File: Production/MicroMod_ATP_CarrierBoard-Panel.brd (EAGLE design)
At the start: 111.5 x 238.8 mm, 873 parts, among them J19 QWIIC_RIGHT_ANGLE, J2 JTAG, J20 QWIIC_RIGHT_ANGLE, J21 1X04_SMD_STRAIGHT_COMBO, J27 MICROMOD-2222-C, J28 USB_A_SMT_FEMALE, J34 QWIIC_RIGHT_ANGLE, J35 QWIIC_RIGHT_ANGLE, J37 1X04_SMD_STRAIGHT_COMBO, J4 USB_A_SMT_FEMALE, J40 1X04_SMD_STRAIGHT_COMBO, J50 JTAG, J51 MICROMOD-2222-C, J52 USB_A_SMT_FEMALE, J58 QWIIC_RIGHT_ANGLE, J59 QWIIC_RIGHT_ANGLE, J6 MICROMOD-2222-C, J61 1X04_SMD_STRAIGHT_COMBO, J64 1X04_SMD_STRAIGHT_COMBO, J7 JTAG, J74 JTAG, J75 MICROMOD-2222-C, J76 USB_A_SMT_FEMALE, J8 1X04_SMD_STRAIGHT_COMBO, J82 QWIIC_RIGHT_ANGLE, J83 QWIIC_RIGHT_ANGLE, J85 1X04_SMD_STRAIGHT_COMBO, J88 1X04_SMD_STRAIGHT_COMBO, U1 AP7361C-33, U2 AP7361C-33, U3 AP7361C-33, U5 AP7361C-33

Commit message: Update panel
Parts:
- added D21: 3.3V, SparkFun-DiscreteSemi:SOD-323
- added D22, D23: RED, SparkFun-LED:LED-0603
- added D24: 1A/15V/220mV, SparkFun-DiscreteSemi:DO-214BA
- D11, D16: value 3A/10V/280mV -> RED; device SparkFun-DiscreteSemi:SOD-323 -> SparkFun-LED:LED-0603
- D12: value 1A/23V/620mV -> 1A/15V/220mV; device SparkFun-DiscreteSemi:SOD-323 -> SparkFun-DiscreteSemi:DO-214BA
- D13: value 3.3V -> 3A/10V/280mV
- D14, D20: value RED -> 1A/23V/620mV; device SparkFun-LED:LED-0603 -> SparkFun-DiscreteSemi:SOD-323
- D15, D9: value RED -> 3.3V; device SparkFun-LED:LED-0603 -> SparkFun-DiscreteSemi:SOD-323
- D17: value 1A/23V/620mV -> RED; device SparkFun-DiscreteSemi:SOD-323 -> SparkFun-LED:LED-0603
- D18: value 3.3V -> 1A/15V/220mV; device SparkFun-DiscreteSemi:SOD-323 -> SparkFun-DiscreteSemi:DO-214BA
- D19: value RED -> 3A/10V/280mV; device SparkFun-LED:LED-0603 -> SparkFun-DiscreteSemi:SOD-323
- D4: value 3A/10V/280mV -> 1A/15V/220mV; device SparkFun-DiscreteSemi:SOD-323 -> SparkFun-DiscreteSemi:DO-214BA
- D5: value 1A/23V/620mV -> 3A/10V/280mV
- D8: value 3.3V -> 1A/23V/620mV
- U$130: device fl3:#VUSB#10 -> buzzard_labels (9):22229
- U$146: device buzzard_labels (9):22229 -> output:#VHOST#0
- U$186, U$331, U$476: device power:#VUSB#10 -> power:#MEAS#10
- U$187, U$332, U$477: device power:#MEAS#10 -> power:#SDA#4
- U$188, U$333, U$478: device power:#SDA#4 -> power:#SWD#10
- U$189, U$334, U$479: device power:#SWD#10 -> headtop:#I2S_CLK#5
- U$190, U$335, U$480: device headtop:#I2S_CLK#5 -> headtop:#DAT1#4
- U$191, U$336, U$481: device headtop:#DAT1#4 -> headtop:#DAT0#4
- U$192, U$337, U$482: device headtop:#DAT0#4 -> headers_dup:#RX2#3
- U$193, U$338, U$483: device headers_dup:#RX2#3 -> headers_dup:#TX2#2
- U$194, U$339, U$484: device headers_dup:#TX2#2 -> headers_dup:#SCL1#3
- U$195, U$340, U$485: device headers_dup:#SCL1#3 -> headers_dup:#SDA1#3
- U$196, U$341, U$486: device headers_dup:#SDA1#3 -> headers_dup:#SCK1#2
- U$197, U$342, U$487: device headers_dup:#SCK1#2 -> headers_dup:VIN3
- U$198, U$343, U$488: device headers_dup:VIN3 -> headers_dup:3V34
- U$199, U$344, U$489: device headers_dup:3V34 -> power:#3V3#1
- U$203, U$348, U$493: device power:#3V3#1 -> headers_dup:ATP0
- U$204, U$349, U$494: device headers_dup:ATP0 -> headers_dup:I2C4
- U$205, U$350, U$495: device headers_dup:I2C4 -> headers_dup:I2C14
- U$206, U$351, U$496: device headers_dup:I2C14 -> headers_dup:ATP_CARRIER_BOARD1
- U$207, U$352, U$497: device headers_dup:ATP_CARRIER_BOARD1 -> fl1:##CS1##0
- U$208, U$353, U$498: device fl1:##CS1##0 -> headers_dup:#CIPO1#2
- U$209, U$354, U$499: device headers_dup:#CIPO1#2 -> headers_dup:#COPI1#2
- U$210, U$355, U$500: device headers_dup:#COPI1#2 -> headers_dup:##CS1##2
- U$211, U$356, U$501: device headers_dup:##CS1##2 -> power:##RESET##7
- U$212, U$357, U$502: device power:##RESET##7 -> headtop:##CS##0
- U$213, U$358, U$503: device headtop:##CS##0 -> fl1:#CIPO1#2
- U$214, U$359, U$504: device fl1:#CIPO1#2 -> fl1:#COPI1#2
- U$215, U$360, U$505: device fl1:#COPI1#2 -> fl1:#RX2#3
- U$216, U$361, U$506: device fl1:#RX2#3 -> fl1:#SCK1#2
- U$217, U$362, U$507: device fl1:#SCK1#2 -> fl1:#SCL1#3
- U$218, U$363, U$508: device fl1:#SCL1#3 -> fl1:#SDA1#3
- U$219, U$364, U$509: device fl1:#SDA1#3 -> fl1:#TX2#2
- U$220, U$365, U$510: device fl1:#TX2#2 -> fl2:##CS##DAT3#0
- U$221, U$366, U$511: device fl2:##CS##DAT3#0 -> fl2:#DAT2#5
- U$222, U$367, U$512: device fl2:#DAT2#5 -> fl2:#DAT1#5
- U$223, U$368, U$513: device fl2:#DAT1#5 -> fl2:#COPI#4
- U$224, U$369, U$514: device fl2:#COPI#4 -> fl2:#SCK#4
- U$225, U$370, U$515: device fl2:#SCK#4 -> fl2:#MCLK#6
- U$226, U$371, U$516: device fl2:#MCLK#6 -> fl2:#I2S_FS#7
- U$227, U$372, U$517: device fl2:#I2S_FS#7 -> fl2:#I2S_CLK#7
- U$228, U$373, U$518: device fl2:#I2S_CLK#7 -> fl2:#RTS#7
- U$229, U$374, U$519: device fl2:#RTS#7 -> fl2:#CTS#8
- U$230, U$375, U$520: device fl2:#CTS#8 -> fl2:#TX#9
- U$231, U$376, U$521: device fl2:#TX#9 -> fl2:#RX#10
- U$232, U$377, U$522: device fl2:#RX#10 -> fl2:#CAN_RX#10
- U$233, U$378, U$523: device fl2:#CAN_RX#10 -> fl2:#CAN_TX#10
- U$234, U$379, U$524: device fl2:#CAN_TX#10 -> fl4:#D0#0
- U$235, U$380, U$525: device fl4:#D0#0 -> fl3:#GND#0
- U$241, U$386, U$531: device fl3:#GND#0 -> fl3:#3V3#1
- U$243, U$388, U$533: device fl3:#3V3#1 -> fl3:#SDA#4
- U$244, U$389, U$534: device fl3:#SDA#4 -> fl3:#SCL#5
- U$245, U$390, U$535: device fl3:#SCL#5 -> fl2:##I2C_INT##10
- U$246, U$391, U$536: device fl2:##I2C_INT##10 -> fl4:#G11#10
- U$247, U$392, U$537: device fl4:#G11#10 -> fl4:#G8#8
- U$248, U$393, U$538: device fl4:#G8#8 -> fl4:#G7#7
- U$249, U$394, U$539: device fl4:#G7#7 -> fl4:#G6#6
- U$250, U$395, U$540: device fl4:#G6#6 -> fl4:#G5#5
- U$251, U$396, U$541: device fl4:#G5#5 -> fl4:#G4#4
- U$252, U$397, U$542: device fl4:#G4#4 -> fl4:#G3#3
- U$253, U$398, U$543: device fl4:#G3#3 -> fl4:#G2#2
- U$254, U$399, U$544: device fl4:#G2#2 -> fl4:#G1#2
- U$255, U$400, U$545: device fl4:#G1#2 -> fl4:#G0#2
- U$256, U$401, U$546: device fl4:#G0#2 -> fl4:#PWM0#10
- U$257, U$402, U$547: device fl4:#PWM0#10 -> fl4:#PWM1#10
- U$258, U$403, U$548: device fl4:#PWM1#10 -> fl4:#A0#10
- U$259, U$404, U$549: device fl4:#A0#10 -> fl4:#A1#10
- U$260, U$405, U$550: device fl4:#A1#10 -> fl3:##RESET##7
- U$261, U$406, U$551: device fl3:##RESET##7 -> fl3:#3V3#1
- U$262, U$407, U$552: device fl3:#3V3#1 -> fl3:#VIN#6
- U$263, U$408, U$553: device fl3:#VIN#6 -> fl3:#HOST_D##9
- U$264, U$409, U$554: device fl3:#HOST_D##9 -> fl3:#HOST_D##10
- U$265, U$410, U$555: device fl3:#HOST_D##10 -> fl3:#SWD#10
- U$266, U$411, U$556: device fl3:#VUSB#10 -> fl3:#MEAS#10
- U$267, U$412, U$557: device fl3:#SWD#10 -> fl3:#VIN_LED#10
- U$268, U$413, U$558: device fl3:#MEAS#10 -> fl3:#3V3_LED#10
- U$269, U$414, U$559: device fl3:#VIN_LED#10 -> fl4:#G9#ADC##CAM_HSYNC#9
- U$270, U$415, U$560: device fl3:#3V3_LED#10 -> fl4:#G10#ADC##CAM_VSYNC#10
- U$271, U$416, U$561: device fl4:#G9#ADC##CAM_HSYNC#9 -> fl2:#I2S_SDI#CAM_PCLK#7
- U$272, U$417, U$562: device fl4:#G10#ADC##CAM_VSYNC#10 -> fl2:#I2S_SDO#CAM_MCLK#7
- U$273, U$418, U$563: device fl2:#I2S_SDI#CAM_PCLK#7 -> fl3:#3V3#1
- U$274, U$419, U$564: device fl2:#I2S_SDO#CAM_MCLK#7 -> headtop:#SCK#2
- U$275, U$420, U$565: device fl3:#3V3#1 -> power:#GND#0
- U$276, U$421, U$566: device headtop:#SCK#2 -> power:#GND#0
- U$278, U$423, U$568: device power:#GND#0 -> headtop:##I2C_INT##10
- U$279, U$424, U$569: device power:#GND#0 -> D1:D10
- U$280, U$425, U$570: device headtop:##I2C_INT##10 -> SparkFun-MicroMod:MICROMOD_MI_LOGO_1
- U$281, U$426, U$571: device D1:D10 -> headtop:MOUNT10
- U$282, U$427, U$572: device SparkFun-MicroMod:MICROMOD_MI_LOGO_1 -> headtop:MOUNT10
- U$285, U$430, U$575: device headtop:MOUNT10 -> SparkFun-MicroMod:MICROMOD_LOGO_1
- U$286, U$431, U$576: device headtop:MOUNT10 -> fl2:#CIPO#DAT0#6
- U$287, U$432, U$577: device SparkFun-MicroMod:MICROMOD_LOGO_1 -> D1_again:D10
- U$288, U$433, U$578: device fl2:#CIPO#DAT0#6 -> output:#EN#0
- U$289, U$434, U$579: device D1_again:D10 -> output:#VHOST#0
- U$290, U$435, U$580: device output:#EN#0 -> output:#VHOST#0
- U$50: device power:#VUSB#10 -> output:#VHOST#0
- moved D11 105.7 mm to (6.60, 63.2)
- moved D17 104.3 mm to (6.60, 119.6)
- moved D16 104.0 mm to (6.60, 121.7)
- moved D4 92.8 mm to (2.72, 26.0), turned to 90 degrees
- moved D12 91.6 mm to (2.72, 82.4), turned to 90 degrees
- moved U$275 78.3 mm to (76.8, 71.6), flipped to the top, turned to 0 degrees
- moved U$420 78.3 mm to (76.8, 128.0), flipped to the top, turned to 0 degrees
- moved U$565 78.3 mm to (76.8, 184.4), flipped to the top, turned to 0 degrees
- moved U$277 72.9 mm to (10.9, 102.7), turned to 90 degrees
- moved U$422 72.9 mm to (10.9, 159.1), turned to 90 degrees
- moved U$567 72.9 mm to (10.9, 215.5), turned to 90 degrees
- moved U$202 70.5 mm to (7.62, 102.9), turned to 90 degrees
- moved U$347 70.5 mm to (7.62, 159.3), turned to 90 degrees
- moved U$492 70.5 mm to (7.62, 215.6), turned to 90 degrees
- moved U$203 68.7 mm to (69.1, 72.1), turned to 0 degrees
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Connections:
- removed net N$19 (its old number): BT3.+, D11.A, R19.1
- removed net N$20 (its old number): D14.A, R23.1
- removed net N$28 (its old number): D19.A, R31.1
- removed net N$29 (its old number): D20.A, R32.1
- removed net N$8 (its old number): BT2.+, D4.A, R11.1
- new net N$16: D11.C, VIN_LED1.1
- new net N$18: D12.C, J28.VBUS, J42.1
- new net N$24: 3V3_LED2.1, D16.C
- new net N$25: D17.C, VIN_LED2.1
- new net N$32: D23.A, R32.1
- new net N$33: 3V3_LED3.1, D22.C
- new net N$34: D23.C, VIN_LED3.1
- new net N$36: D24.C, J76.VBUS, J90.1
- new net N$7: D4.C, J11.1, J4.VBUS
- net 3.3V1: now also D8.A; no longer D5.A
- net 3.3V2: now also D14.A; no longer D12.A
- net 3.3V3: now also D20.A; no longer D17.A
- net 3.3V_EN1: now also D9.C; no longer D8.C
- net 3.3V_EN2: now also D15.C; no longer D13.C
- net 3.3V_EN3: now also D21.C; no longer D18.C
- net GND1: now also D9.A; no longer D8.A
- net GND2: now also D15.A; no longer D13.A
- net GND3: now also D21.A; no longer D18.A
- net N$12: now also R15.1; no longer R16.1
- net N$13: now also D11.A, R16.1; no longer 3V3_LED1.1, D9.C
- net N$15: now also 3V3_LED1.1; no longer VIN_LED1.1
- net N$21: now also BT3.+, D13.A, R19.1; no longer D15.A, R24.1
- net N$22: now also D16.A, R23.1; no longer 3V3_LED2.1, D14.C
- net N$23: now also D17.A, R24.1; no longer D15.C, VIN_LED2.1
- net N$27: now also D18.C, J52.VBUS, J66.1; no longer BT4.+, D16.A, R27.1
- net N$30: now also BT4.+, D19.A, R27.1; no longer 3V3_LED3.1, D19.C
- net N$31: now also D22.A, R31.1; no longer D20.C, VIN_LED3.1
- net N$9: now also BT2.+, D5.A, R11.1; no longer D9.A, R15.1
- net RTC_3V1: now also D8.C; no longer D4.C
- net RTC_3V2: now also D13.C, D14.C; no longer D11.C, D12.C
- net RTC_3V3: now also D19.C, D20.C; no longer D16.C, D17.C
- net V_USB: now also D4.A; no longer J11.1, J4.VBUS
- net V_USB1: now also D12.A; no longer J28.VBUS, J42.1
- net V_USB2: now also D18.A; no longer J52.VBUS, J66.1
- net V_USB3: now also D24.A; no longer J76.VBUS, J90.1
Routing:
- net N$36: track 0.00 -> 25.8 mm
- net N$18: track 0.00 -> 25.8 mm
- net N$7: track 0.00 -> 25.8 mm
- net N$27: track 4.10 -> 25.8 mm
- net V_USB1: track 45.7 -> 25.5 mm
- net V_USB: track 45.7 -> 25.5 mm
- net V_USB2: track 45.7 -> 25.5 mm
- net V_USB3: track 45.7 -> 25.5 mm
- net N$19 (its old number): track 4.10 -> 0.00 mm
- net N$8 (its old number): track 4.10 -> 0.00 mm
- net N$34: track 0.00 -> 2.67 mm, vias 0 -> 1
- net N$33: track 0.00 -> 2.67 mm, vias 0 -> 1
- net N$25: track 0.00 -> 2.67 mm, vias 0 -> 1
- net N$24: track 0.00 -> 2.67 mm, vias 0 -> 1
- net N$16: track 0.00 -> 2.67 mm, vias 0 -> 1
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
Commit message: Changes production board size to 2x2 instead of 1x4
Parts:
- moved BYP3 143.9 mm to (100.8, 84.0)
- moved C22 143.9 mm to (104.1, 69.6)
- moved C23 143.9 mm to (105.7, 69.6)
- moved C24 143.9 mm to (107.2, 69.6)
- moved D19 143.9 mm to (153.9, 95.2)
- moved D24 143.9 mm to (92.1, 82.4)
- moved FD14 143.9 mm to (171.1, 107.7)
- moved FD16 143.9 mm to (171.1, 107.7)
- moved H24 143.9 mm to (173.2, 58.9)
- moved J75 143.9 mm to (125.0, 84.3)
- moved LOGO24 143.9 mm to (153.2, 83.2)
- moved LOGO28 143.9 mm to (157.7, 79.8)
- moved R25 143.9 mm to (97.0, 76.7)
- moved R27 143.9 mm to (153.9, 96.9)
- moved R28 143.9 mm to (105.2, 78.2)
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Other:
- board size 111.5 x 238.8 mm -> 200.9 x 126 mm

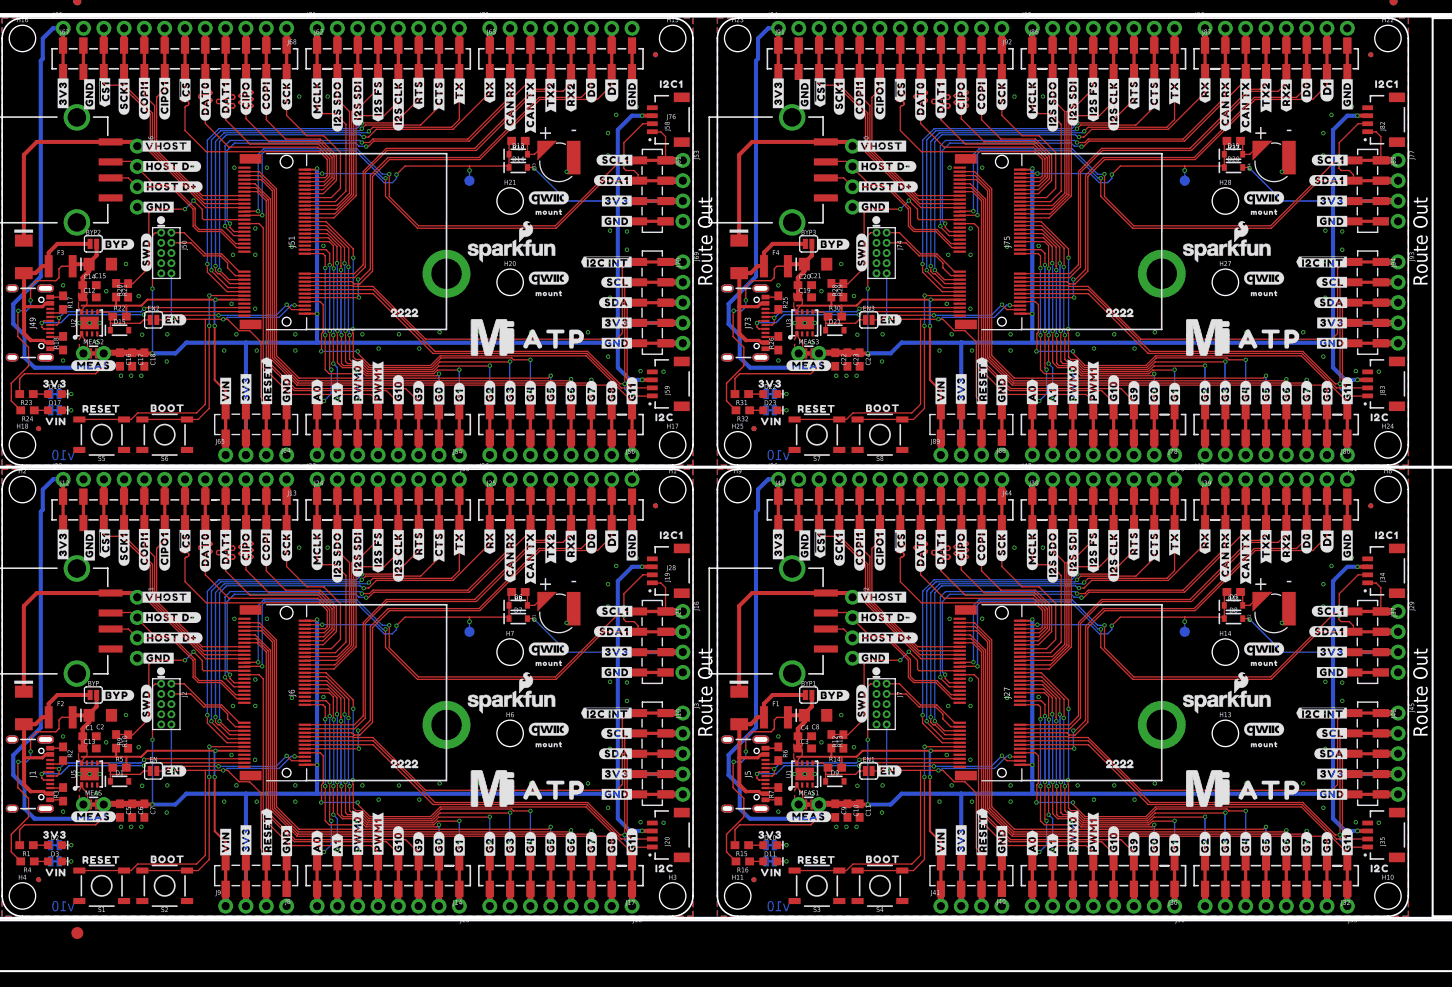
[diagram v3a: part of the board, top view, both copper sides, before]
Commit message: Updates production files with new silk and qwiic connector fixes
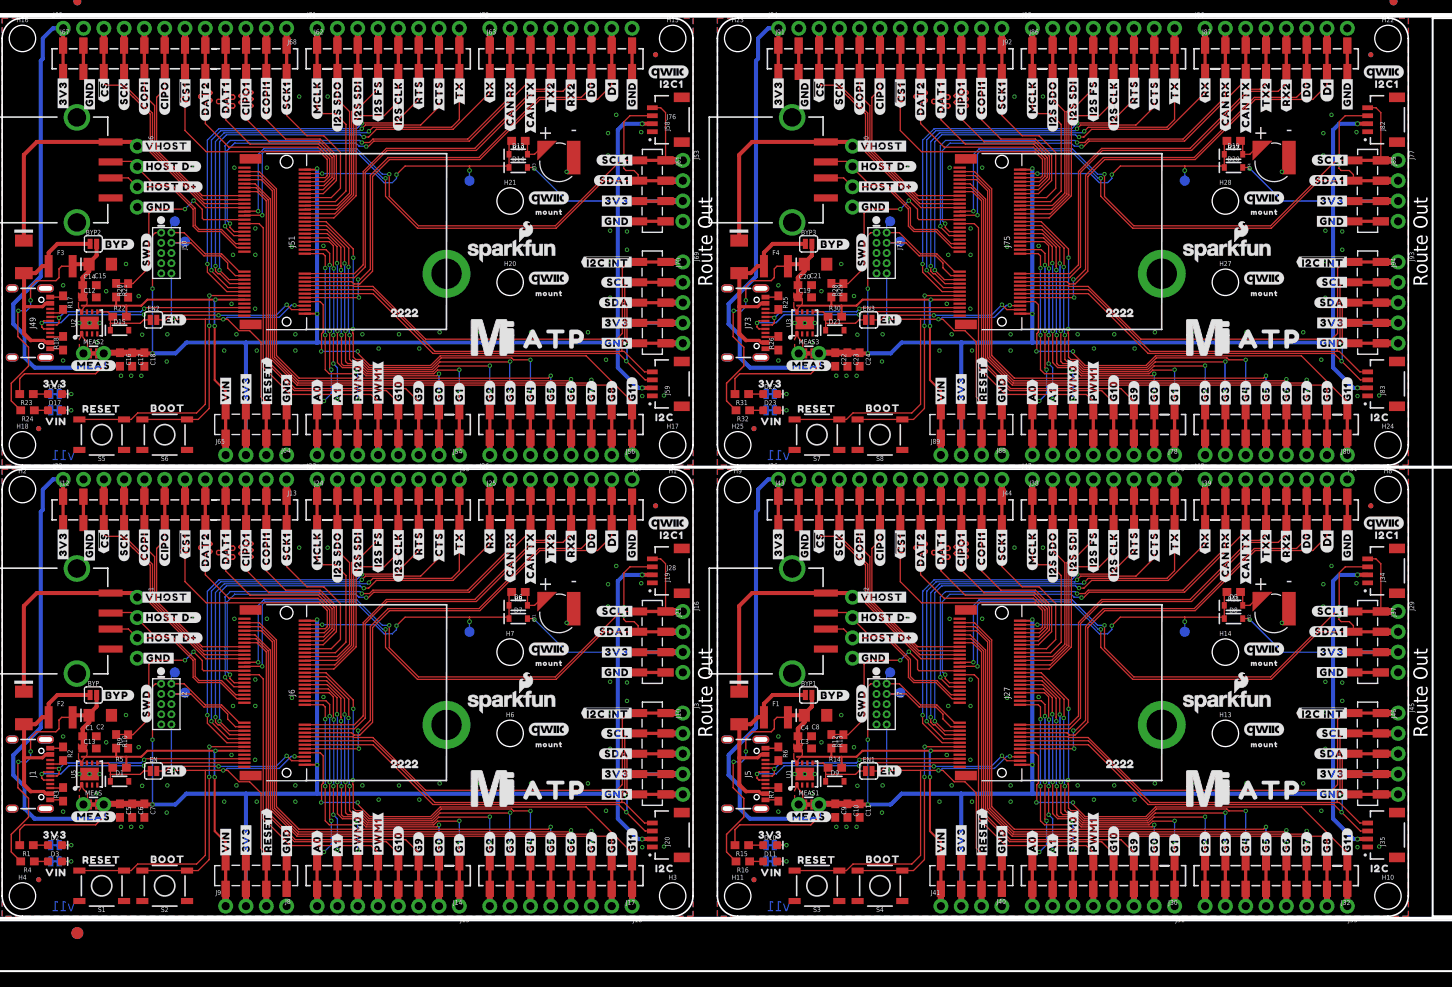
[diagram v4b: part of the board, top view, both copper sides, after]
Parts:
- added E$6: (no value), SparkFun-Retired:FIDUCIAL-1.5X3
- added LOGO29, LOGO30, LOGO32: QWIIC_LOGO_3MM, SparkFun-Aesthetics:QWIIC_5MM
- added LOGO31: QWIIC_LOGO_5MM, SparkFun-Aesthetics:QWIIC_5MM
- added TP10, TP11, TP12, TP5, TP6, TP7, TP8, TP9: TEST-POINT3X5, SparkFun-Connectors:PAD.03X.05
- LOGO10: value SFE_LOGO_NAME_FLAME.1_INCH -> SFE_LOGO_NAME_FLAME.2_INCH; device SparkFun-Aesthetics:SFE_LOGO_NAME_FLAME_.1 -> SparkFun-Aesthetics:SFE_LOGO_NAME_FLAME_.2
- LOGO11, LOGO19, LOGO27: value QWIIC_LOGO_3MM -> SFE_LOGO_NAME_FLAME.1_INCH; device SparkFun-Aesthetics:QWIIC_5MM -> SparkFun-Aesthetics:SFE_LOGO_NAME_FLAME_.1
- LOGO14, LOGO21, LOGO28: value QWIIC_LOGO_5MM -> QWIIC_LOGO_3MM
- LOGO15: value OSHW-LOGOMINI -> QWIIC_LOGO_5MM; device SparkFun-Aesthetics:OSHW-LOGO-MINI -> SparkFun-Aesthetics:QWIIC_5MM
- LOGO16: value SFE_LOGO_NAME_FLAME.2_INCH -> QWIIC_LOGO_3MM; device SparkFun-Aesthetics:SFE_LOGO_NAME_FLAME_.2 -> SparkFun-Aesthetics:QWIIC_5MM
- LOGO17: value SFE_LOGO_NAME_FLAME.1_INCH -> OSHW-LOGOMINI; device SparkFun-Aesthetics:SFE_LOGO_NAME_FLAME_.1 -> SparkFun-Aesthetics:OSHW-LOGO-MINI
- LOGO18, LOGO26: value QWIIC_LOGO_3MM -> SFE_LOGO_NAME_FLAME.2_INCH; device SparkFun-Aesthetics:QWIIC_5MM -> SparkFun-Aesthetics:SFE_LOGO_NAME_FLAME_.2
- LOGO22, LOGO7: value OSHW-LOGOMINI -> QWIIC_LOGO_3MM; device SparkFun-Aesthetics:OSHW-LOGO-MINI -> SparkFun-Aesthetics:QWIIC_5MM
- LOGO23: value SFE_LOGO_NAME_FLAME.2_INCH -> QWIIC_LOGO_5MM; device SparkFun-Aesthetics:SFE_LOGO_NAME_FLAME_.2 -> SparkFun-Aesthetics:QWIIC_5MM
- LOGO24: value SFE_LOGO_NAME_FLAME.1_INCH -> QWIIC_LOGO_3MM; device SparkFun-Aesthetics:SFE_LOGO_NAME_FLAME_.1 -> SparkFun-Aesthetics:QWIIC_5MM
- LOGO25: value QWIIC_LOGO_3MM -> OSHW-LOGOMINI; device SparkFun-Aesthetics:QWIIC_5MM -> SparkFun-Aesthetics:OSHW-LOGO-MINI
- LOGO9: value SFE_LOGO_NAME_FLAME.2_INCH -> OSHW-LOGOMINI; device SparkFun-Aesthetics:SFE_LOGO_NAME_FLAME_.2 -> SparkFun-Aesthetics:OSHW-LOGO-MINI
- U$130: device buzzard_labels (9):22229 -> headtop:#CAN_RX#9
- U$147: device headtop:#CAN_RX#9 -> alc:#CIPO#5178038
- U$190, U$335, U$480: device headtop:#DAT1#4 -> headers_dup:#RX2#3
- U$191, U$336, U$481: device headtop:#DAT0#4 -> headers_dup:#TX2#2
- U$192, U$337, U$482: device headers_dup:#RX2#3 -> headers_dup:#SCL1#3
- U$193, U$338, U$483: device headers_dup:#TX2#2 -> headers_dup:#SDA1#3
- U$194, U$339, U$484: device headers_dup:#SCL1#3 -> headers_dup:#SCK1#2
- U$195, U$340, U$485: device headers_dup:#SDA1#3 -> headers_dup:VIN3
- U$196, U$341, U$486: device headers_dup:#SCK1#2 -> headers_dup:3V34
- U$197, U$342, U$487: device headers_dup:VIN3 -> power:#3V3#1
- U$198, U$343, U$488: device headers_dup:3V34 -> power:#3V3#1
- U$20: device headers_dup:##CS1##2 -> alc:##CS1##5178039
- U$201, U$346, U$491: device power:#3V3#1 -> headers_dup:ATP0
- U$202, U$347, U$492: device power:#3V3#1 -> headers_dup:I2C4
- U$203, U$348, U$493: device headers_dup:ATP0 -> headers_dup:I2C14
- U$204, U$349, U$494: device headers_dup:I2C4 -> headers_dup:ATP_CARRIER_BOARD1
- U$205, U$350, U$495: device headers_dup:I2C14 -> headers_dup:#COPI1#2
- U$206, U$351, U$496: device headers_dup:ATP_CARRIER_BOARD1 -> power:##RESET##7
- U$207, U$352, U$497: device fl1:##CS1##0 -> headtop:##CS##0
- U$208, U$353, U$498: device headers_dup:#CIPO1#2 -> fl1:#COPI1#2
- U$209, U$354, U$499: device headers_dup:#COPI1#2 -> fl1:#RX2#3
- U$210, U$355, U$500: device headers_dup:##CS1##2 -> fl1:#SCK1#2
- U$211, U$356, U$501: device power:##RESET##7 -> fl1:#SCL1#3
- U$212, U$357, U$502: device headtop:##CS##0 -> fl1:#SDA1#3
- U$213, U$358, U$503: device fl1:#CIPO1#2 -> fl1:#TX2#2
- U$214, U$359, U$504: device fl1:#COPI1#2 -> fl2:#DAT2#5
- U$215, U$360, U$505: device fl1:#RX2#3 -> fl2:#DAT1#5
- U$216, U$361, U$506: device fl1:#SCK1#2 -> fl2:#COPI#4
- U$217, U$362, U$507: device fl1:#SCL1#3 -> fl2:#SCK#4
- U$218, U$363, U$508: device fl1:#SDA1#3 -> fl2:#MCLK#6
- U$219, U$364, U$509: device fl1:#TX2#2 -> fl2:#I2S_FS#7
- U$220, U$365, U$510: device fl2:##CS##DAT3#0 -> fl2:#I2S_CLK#7
- U$221, U$366, U$511: device fl2:#DAT2#5 -> fl2:#RTS#7
- U$222, U$367, U$512: device fl2:#DAT1#5 -> fl2:#CTS#8
- U$223, U$368, U$513: device fl2:#COPI#4 -> fl2:#TX#9
- U$224, U$369, U$514: device fl2:#SCK#4 -> fl2:#RX#10
- U$225, U$370, U$515: device fl2:#MCLK#6 -> fl2:#CAN_RX#10
- U$226, U$371, U$516: device fl2:#I2S_FS#7 -> fl2:#CAN_TX#10
- U$227, U$372, U$517: device fl2:#I2S_CLK#7 -> fl4:#D0#0
- U$228, U$373, U$518: device fl2:#RTS#7 -> fl3:#GND#0
- U$229, U$374, U$519: device fl2:#CTS#8 -> fl3:#GND#0
- U$230, U$375, U$520: device fl2:#TX#9 -> fl3:#GND#0
- U$231, U$376, U$521: device fl2:#RX#10 -> fl3:#GND#0
- U$232, U$377, U$522: device fl2:#CAN_RX#10 -> fl3:#GND#0
- U$233, U$378, U$523: device fl2:#CAN_TX#10 -> fl3:#GND#0
- U$234, U$379, U$524: device fl4:#D0#0 -> fl3:#3V3#1
- U$235, U$380, U$525: device fl3:#GND#0 -> fl3:#3V3#1
- U$236, U$381, U$526: device fl3:#GND#0 -> fl3:#SDA#4
- U$237, U$382, U$527: device fl3:#GND#0 -> fl3:#SCL#5
- U$238, U$383, U$528: device fl3:#GND#0 -> fl2:##I2C_INT##10
- U$239, U$384, U$529: device fl3:#GND#0 -> fl4:#G11#10
- U$240, U$385, U$530: device fl3:#GND#0 -> fl4:#G8#8
- U$241, U$386, U$531: device fl3:#3V3#1 -> fl4:#G7#7
- U$242, U$387, U$532: device fl3:#3V3#1 -> fl4:#G6#6
- U$243, U$388, U$533: device fl3:#SDA#4 -> fl4:#G5#5
- U$244, U$389, U$534: device fl3:#SCL#5 -> fl4:#G4#4
- U$245, U$390, U$535: device fl2:##I2C_INT##10 -> fl4:#G3#3
- U$246, U$391, U$536: device fl4:#G11#10 -> fl4:#G2#2
- U$247, U$392, U$537: device fl4:#G8#8 -> fl4:#G1#2
- U$248, U$393, U$538: device fl4:#G7#7 -> fl4:#G0#2
- U$249, U$394, U$539: device fl4:#G6#6 -> fl4:#PWM0#10
- U$250, U$395, U$540: device fl4:#G5#5 -> fl4:#PWM1#10
- U$251, U$396, U$541: device fl4:#G4#4 -> fl4:#A0#10
- U$252, U$397, U$542: device fl4:#G3#3 -> fl4:#A1#10
- U$253, U$398, U$543: device fl4:#G2#2 -> fl3:##RESET##7
- U$254, U$399, U$544: device fl4:#G1#2 -> fl3:#3V3#1
- U$255, U$400, U$545: device fl4:#G0#2 -> fl3:#VIN#6
- U$256, U$401, U$546: device fl4:#PWM0#10 -> fl3:#HOST_D##9
- U$257, U$402, U$547: device fl4:#PWM1#10 -> fl3:#HOST_D##10
- U$258, U$403, U$548: device fl4:#A0#10 -> fl3:#SWD#10
- U$259, U$404, U$549: device fl4:#A1#10 -> fl3:#MEAS#10
- U$260, U$405, U$550: device fl3:##RESET##7 -> fl3:#VIN_LED#10
- U$261, U$406, U$551: device fl3:#3V3#1 -> fl3:#3V3_LED#10
- U$262, U$407, U$552: device fl3:#VIN#6 -> fl4:#G9#ADC##CAM_HSYNC#9
- U$263, U$408, U$553: device fl3:#HOST_D##9 -> fl4:#G10#ADC##CAM_VSYNC#10
- U$264, U$409, U$554: device fl3:#HOST_D##10 -> fl2:#I2S_SDI#CAM_PCLK#7
- U$265, U$410, U$555: device fl3:#SWD#10 -> fl2:#I2S_SDO#CAM_MCLK#7
- U$266, U$411, U$556: device fl3:#MEAS#10 -> fl3:#3V3#1
- U$267, U$412, U$557: device fl3:#VIN_LED#10 -> headtop:#SCK#2
- U$268, U$413, U$558: device fl3:#3V3_LED#10 -> power:#GND#0
- U$269, U$414, U$559: device fl4:#G9#ADC##CAM_HSYNC#9 -> power:#GND#0
- U$270, U$415, U$560: device fl4:#G10#ADC##CAM_VSYNC#10 -> power:#GND#0
- U$271, U$416, U$561: device fl2:#I2S_SDI#CAM_PCLK#7 -> headtop:##I2C_INT##10
- U$272, U$417, U$562: device fl2:#I2S_SDO#CAM_MCLK#7 -> D1:D10
- U$273, U$418, U$563: device fl3:#3V3#1 -> SparkFun-MicroMod:MICROMOD_MI_LOGO_1
- U$274, U$419, U$564: device headtop:#SCK#2 -> headtop:MOUNT10
- U$275, U$276, U$277, U$420, U$421, U$422, U$565, U$566, U$567: device power:#GND#0 -> headtop:MOUNT10
- U$278, U$423, U$568: device headtop:##I2C_INT##10 -> SparkFun-MicroMod:MICROMOD_LOGO_1
- U$279, U$424, U$569: device D1:D10 -> D1_again:D10
- U$280, U$425, U$570: device SparkFun-MicroMod:MICROMOD_MI_LOGO_1 -> output:#EN#0
- U$281, U$282, U$426, U$427, U$571, U$572: device headtop:MOUNT10 -> output:#VHOST#0
- U$283, U$428, U$573: device headtop:MOUNT10 -> alc:##CS##5178037
- U$284, U$429, U$574: device headtop:MOUNT10 -> alc:##CS1##DAT3#5178037
- U$285, U$430, U$575: device SparkFun-MicroMod:MICROMOD_LOGO_1 -> alc:#CIPO#5178038
- U$286, U$431, U$576: device fl2:#CIPO#DAT0#6 -> alc:##CS1##5178039
- U$287, U$432, U$577: device D1_again:D10 -> alc:#DAT1#5178039
- U$288, U$433, U$578: device output:#EN#0 -> alc:#DAT2#5178039
- U$289, U$434, U$579: device output:#VHOST#0 -> alc:#CIPO1#5178039
- U$290, U$435, U$580: device output:#VHOST#0 -> alc:##CIPO1##DAT0#5178038
- U$36: device fl1:##CS1##0 -> alc:#DAT1#5178039
- U$53: device headtop:#DAT1#4 -> alc:#DAT2#5178039
- U$54: device headtop:#DAT0#4 -> alc:#CIPO1#5178039
- U$56: device headers_dup:#CIPO1#2 -> alc:##CIPO1##DAT0#5178038
- U$74: device fl1:#CIPO1#2 -> buzzard_labels (9):22229
- U$81: device fl2:##CS##DAT3#0 -> alc:##CS##5178037
- U$84: device fl2:#CIPO#DAT0#6 -> alc:##CS1##DAT3#5178037
- moved LOGO15 160.1 mm to (157.7, 23.4)
- moved LOGO16 142.4 mm to (172.7, 49.2), flipped to the top
- moved U$147 132.7 mm to (20.3, 51.7), flipped to the bottom, turned to 270 degrees
- moved TP2 126.3 mm to (21.6, 30.5)
- moved U$74 121.1 mm to (137.0, 19.1), flipped to the top, turned to 0 degrees
- moved U$347 85.4 mm to (82.8, 62.4), turned to 0 degrees
- moved U$202 85.4 mm to (172.2, 5.97), turned to 0 degrees
- moved U$492 85.4 mm to (172.2, 62.4), turned to 0 degrees
- moved U$239 83.9 mm to (168.1, 3.56)
- moved U$384 83.9 mm to (78.7, 59.9)
- moved U$529 83.9 mm to (168.1, 59.9)
- moved U$195 76.0 mm to (96.1, 5.46)
- moved U$340 76.0 mm to (6.73, 61.8)
- moved U$485 76.0 mm to (96.1, 61.8)
- moved U$200 74.9 mm to (97.0, 46.5), turned to 90 degrees
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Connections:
- net !CS!/DAT1 renamed !CS1!/DAT1
- net !CS!/DAT2 renamed !CS1!/DAT2
- net !CS!/DAT3 renamed !CS1!/DAT3
- net !CS!/DAT4 renamed !CS1!/DAT4
- net !CS1 renamed !CS!
- net !CS2 renamed !CS!1
- net !CS3 renamed !CS!2
- net !CS4 renamed !CS!3
- net CIPO/DAT0 renamed CIPO1/DAT0
- net CIPO/DAT1 renamed CIPO1/DAT1
- net CIPO/DAT2 renamed CIPO1/DAT2
- net CIPO/DAT3 renamed CIPO1/DAT3
- removed net CIPO4: J75.61, J91.6, J92.7
- new net CIPO: J12.6, J13.7, J6.61
- net 3.3V: now also J19.2, J20.2; no longer J19.3, J20.3
- net 3.3V1: now also J34.2, J35.2; no longer J34.3, J35.3
- net 3.3V2: now also J58.2, J59.2; no longer J58.3, J59.3
- net 3.3V3: now also J82.2, J83.2; no longer J82.3, J83.3
- net CIPO1: now also J27.61, J43.6, J44.7; no longer J12.6, J13.7, J6.61
- net CIPO2: now also J51.61, J67.6, J68.7; no longer J27.61, J43.6, J44.7
- net CIPO3: now also J75.61, J91.6, J92.7; no longer J51.61, J67.6, J68.7
- net COPI: now also J12.5, J13.8, J6.59; no longer J12.11, J13.2, J6.62
- net COPI1: now also J12.11, J13.2, J6.62; no longer J12.5, J13.8, J6.59
- net COPI2: now also J27.59, J43.5, J44.8; no longer J27.62, J43.11, J44.2
- net COPI3: now also J27.62, J43.11, J44.2; no longer J27.59, J43.5, J44.8
- net COPI4: now also J51.59, J67.5, J68.8; no longer J51.62, J67.11, J68.2
- net COPI5: now also J51.62, J67.11, J68.2; no longer J51.59, J67.5, J68.8
- net COPI6: now also J75.59, J91.5, J92.8; no longer J75.62, J91.11, J92.2
- net COPI7: now also J75.62, J91.11, J92.2; no longer J75.59, J91.5, J92.8
- net GND: now also J19.1, J20.1; no longer J19.4, J20.4
- net GND1: now also J34.1, J35.1; no longer J34.4, J35.4
- net GND2: now also J58.1, J59.1; no longer J58.4, J59.4
- net GND3: now also J82.1, J83.1; no longer J82.4, J83.4
- net RTC_3V1: now also TP4.P$1; no longer TP2.P$1
- net RTC_3V2: now also TP7.P$1; no longer TP3.P$1
- net RTC_3V3: now also TP10.P$1; no longer TP4.P$1
- net SCK: now also J12.4, J22.4, J6.57; no longer J12.12, J13.1, J6.60
- net SCK1: now also J12.12, J13.1, J6.60; no longer J12.4, J22.4, J6.57
- net SCK2: now also J27.57, J36.4, J43.4; no longer J27.60, J43.12, J44.1
- net SCK3: now also J27.60, J43.12, J44.1; no longer J27.57, J36.4, J43.4
- net SCK4: now also J51.57, J60.4, J67.4; no longer J51.60, J67.12, J68.1
- net SCK5: now also J51.60, J67.12, J68.1; no longer J51.57, J60.4, J67.4
- net SCK6: now also J75.57, J84.4, J91.4; no longer J75.60, J91.12, J92.1
- net SCK7: now also J75.60, J91.12, J92.1; no longer J75.57, J84.4, J91.4
- net SCL: now also J20.4; no longer J20.1
- net SCL1: now also J19.4; no longer J19.1
- net SCL2: now also J35.4; no longer J35.1
- net SCL3: now also J34.4; no longer J34.1
- net SCL4: now also J59.4; no longer J59.1
- net SCL5: now also J58.4; no longer J58.1
- net SCL6: now also J83.4; no longer J83.1
- net SCL7: now also J82.4; no longer J82.1
- net SDA: now also J20.3; no longer J20.2
- net SDA1: now also J19.3; no longer J19.2
- net SDA2: now also J35.3; no longer J35.2
- net SDA3: now also J34.3; no longer J34.2
- net SDA4: now also J59.3; no longer J59.2
- net SDA5: now also J58.3; no longer J58.2
- net SDA6: now also J83.3; no longer J83.2
- net SDA7: now also J82.3; no longer J82.2
- net SWDCK: now also TP3.P$1
- net SWDCK1: now also TP6.P$1
- net SWDCK2: now also TP9.P$1
- net SWDCK3: now also TP12.P$1
- net SWDIO: now also TP2.P$1
- net SWDIO1: now also TP5.P$1
- net SWDIO2: now also TP8.P$1
- net SWDIO3: now also TP11.P$1
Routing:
- net CIPO: track 0.00 -> 29.0 mm
- net CIPO4: track 29.0 -> 0.00 mm
- net SCL: track 69.0 -> 63.5 mm, vias 2 -> 0
- net SCL4: track 69.0 -> 63.5 mm, vias 2 -> 0
- net SCL2: track 69.0 -> 63.5 mm, vias 2 -> 0
- net SCL6: track 69.0 -> 63.5 mm, vias 2 -> 0
- net SDA2: track 65.9 -> 62.0 mm, vias 0 -> 2
- net SDA4: track 65.9 -> 62.0 mm, vias 0 -> 2
- net SDA: track 65.9 -> 62.0 mm, vias 0 -> 2
- net SDA6: track 65.9 -> 62.0 mm, vias 0 -> 2
- net SCL1: track 78.3 -> 81.3 mm
- net SCL7: track 78.3 -> 81.3 mm
- net SCL5: track 78.3 -> 81.3 mm
- net SCL3: track 78.3 -> 81.3 mm
- net COPI7: track 29.6 -> 32.0 mm
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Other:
- board text added: "v11"
- board text removed: "v10"
